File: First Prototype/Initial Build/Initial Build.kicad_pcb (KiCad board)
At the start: 2 copper layers, 33 parts, among them J2 Conn_02x04_Odd_Even, Q1 MPSA44, Q2 BC328, Q3 BC517, U1 TLC555xP, U2 TLC555xP

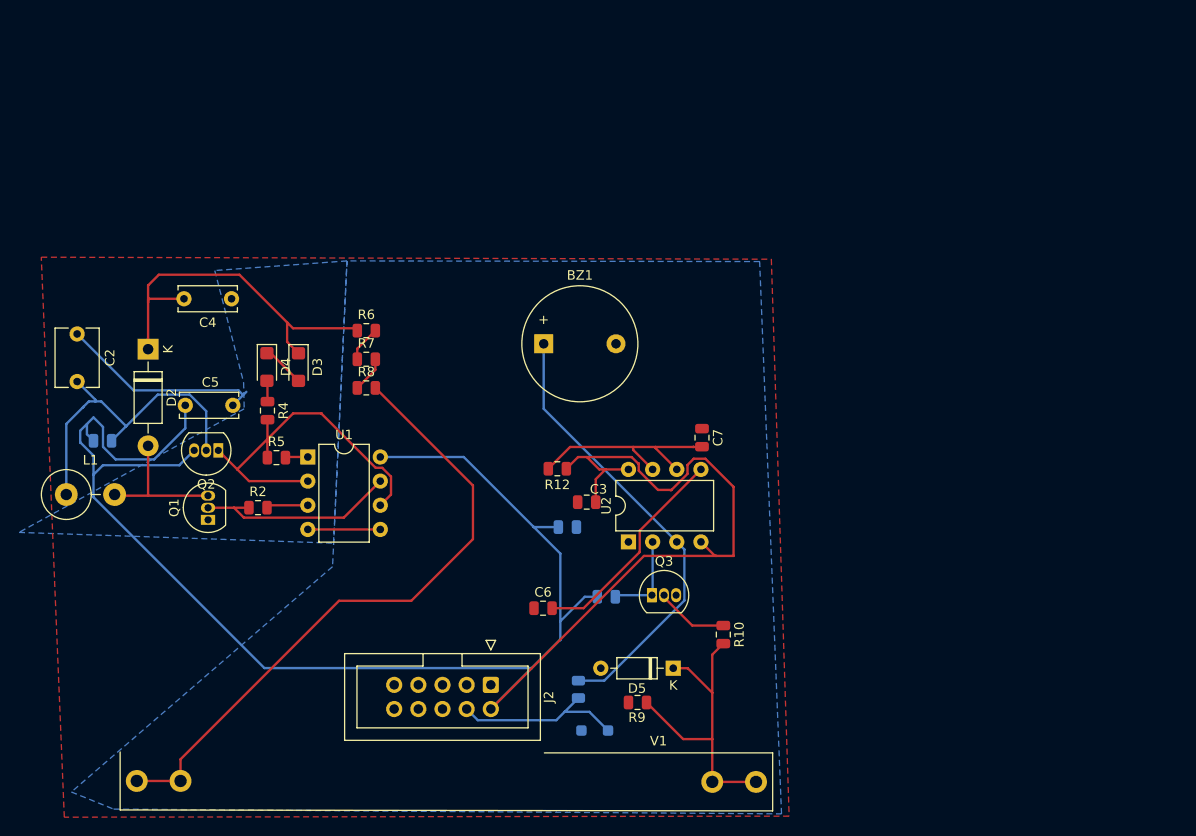
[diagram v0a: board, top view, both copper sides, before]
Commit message: updated tube fp began routing
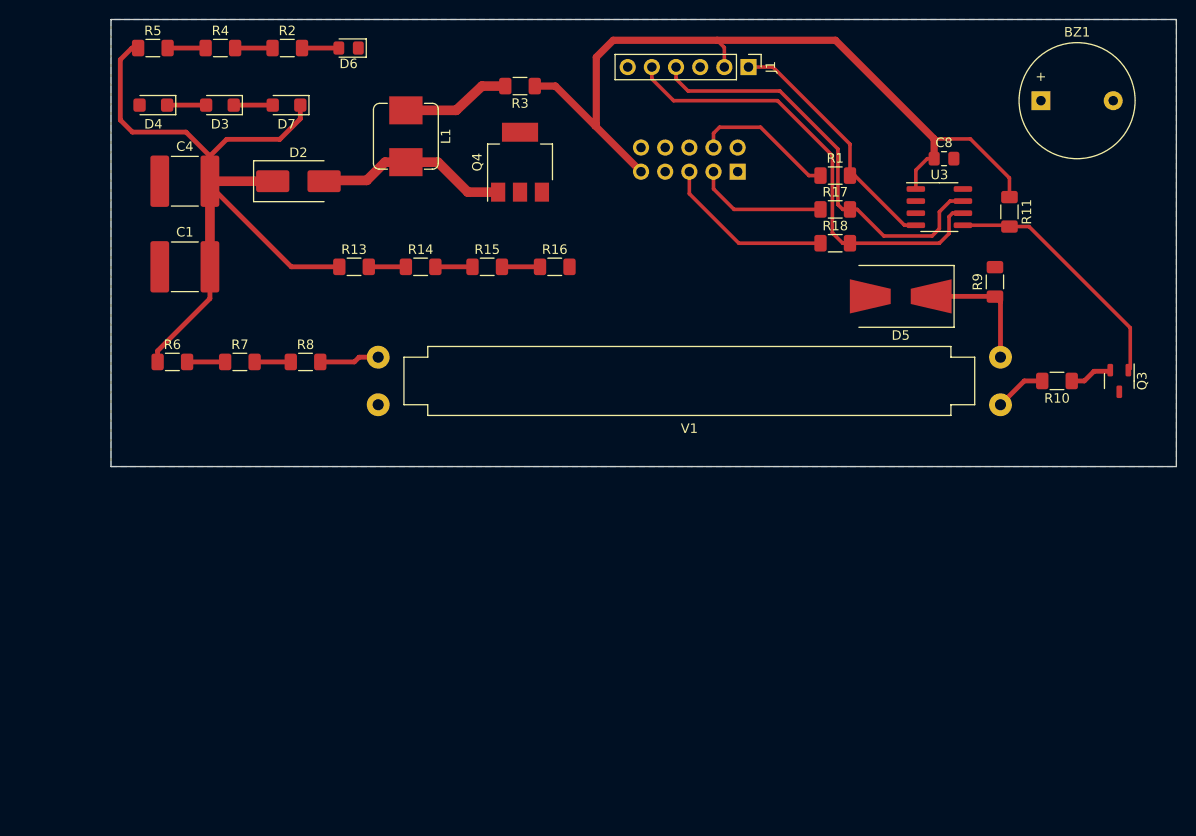
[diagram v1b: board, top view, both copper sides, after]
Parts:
- removed C2: 100n, Capacitor_THT:C_Disc_D6.0mm_W4.4mm_P5.00mm
- removed C3, C6, C7: 100n, Capacitor_SMD:C_0805_2012Metric
- removed C5: 100u, Capacitor_THT:C_Disc_D6.0mm_W2.5mm_P5.00mm
- removed D1: 3v3, Diode_SMD:D_SOD-123F
- removed Q1: MPSA44, Package_TO_SOT_THT:TO-92_Inline
- removed Q2: BC328, Package_TO_SOT_THT:TO-92_Inline
- removed R12: 3k9, Capacitor_SMD:C_0805_2012Metric
- removed U1, U2: TLC555xP, Package_DIP:DIP-8_W7.62mm
- added C8: .1u, Capacitor_SMD:C_0805_2012Metric_Pad1.18x1.45mm_HandSolder, F.Cu at (180.6, 87.6)
- added D6: APTD2012LSURCK, LED_SMD:LED_0805_2012Metric_Pad1.15x1.40mm_HandSolder, F.Cu at (118.0, 76.0)
- added D7: BZD27C150P-E3-08, Diode_SMD:D_SMF, F.Cu at (111.5, 82.0)
- added J1: Conn_01x06, Connector_PinHeader_2.54mm:PinHeader_1x06_P2.54mm_Vertical, F.Cu at (160.0, 78.0)
- added Q4: BSP135H6327XTSA1, Package_TO_SOT_SMD:SOT-223, F.Cu at (136.0, 88.0)
- added R13: 330k, Resistor_SMD:R_1206_3216Metric_Pad1.30x1.75mm_HandSolder, F.Cu at (118.5, 99.0)
- added R14: 330k, Resistor_SMD:R_1206_3216Metric_Pad1.30x1.75mm_HandSolder, F.Cu at (125.5, 99.0)
- added R15: 330k, Resistor_SMD:R_1206_3216Metric_Pad1.30x1.75mm_HandSolder, F.Cu at (132.6, 99.0)
- added R16: 3k9, Resistor_SMD:R_1206_3216Metric_Pad1.30x1.75mm_HandSolder, F.Cu at (139.7, 99.0)
- added R17: 10k, Resistor_SMD:R_1206_3216Metric_Pad1.30x1.75mm_HandSolder, F.Cu at (169.1, 93.0)
- added R18: 10k, Resistor_SMD:R_1206_3216Metric_Pad1.30x1.75mm_HandSolder, F.Cu at (169.1, 96.5)
- added U3: PIC12F1572T-I/SN, Package_SO:SOIC-8_3.9x4.9mm_P1.27mm, F.Cu at (180.1, 92.7)
- C1: value 100n -> LDEPD2100KA5N00; footprint Capacitor_SMD:C_0805_2012Metric -> Capacitor_SMD:C_2220_5650Metric_Pad1.97x5.40mm_HandSolder; moved to F.Cu
- C4: value 47n -> LDEPD2100KA5N00; footprint Capacitor_THT:C_Disc_D6.0mm_W2.5mm_P5.00mm -> Capacitor_SMD:C_2220_5650Metric_Pad1.97x5.40mm_HandSolder
- D2: value MUR160 -> MURS160-13-F; footprint Diode_THT:D_DO-41_SOD81_P10.16mm_Horizontal -> Diode_SMD:D_SMB_Handsoldering
- D3, D4: value 200v -> BZD27C150P-E3-08
- D5: footprint Diode_THT:D_DO-35_SOD27_P7.62mm_Horizontal -> Diode_SMD:D_SMB-SMC_Universal_Handsoldering
- J2: value Conn_02x04_Odd_Even -> Conn_01x10_Pin; footprint Connector_IDC:IDC-Header_2x05_P2.54mm_Vertical -> Connector_PinHeader_2.54mm:PinHeader_2x05_P2.54mm_Vertical; moved to B.Cu
- L1: value 10m -> SRR6603-103ML; footprint Inductor_THT:L_Axial_L12.0mm_D5.0mm_P5.08mm_Vertical_Fastron_MISC -> Inductor_SMD:L_Bourns_SRP7028A_7.3x6.6mm
- Q3: value BC517 -> MMBT3904-7-F; footprint Package_TO_SOT_THT:TO-92_Inline -> Package_TO_SOT_SMD:SOT-23-3
- R1: value 3k3 -> 10k; footprint Resistor_SMD:R_0805_2012Metric -> Resistor_SMD:R_1206_3216Metric_Pad1.30x1.75mm_HandSolder; moved to F.Cu
- R10, R6, R7, R8, R9: footprint Capacitor_SMD:C_0805_2012Metric -> Resistor_SMD:R_1206_3216Metric_Pad1.30x1.75mm_HandSolder
- R11, R3: footprint Capacitor_SMD:C_0805_2012Metric -> Resistor_SMD:R_1206_3216Metric_Pad1.30x1.75mm_HandSolder; moved to F.Cu
- R2: value 1k5 -> 1M8; footprint Capacitor_SMD:C_0805_2012Metric -> Resistor_SMD:R_1206_3216Metric_Pad1.30x1.75mm_HandSolder
- R4: value 10k -> 1M8; footprint Capacitor_SMD:C_0805_2012Metric -> Resistor_SMD:R_1206_3216Metric_Pad1.30x1.75mm_HandSolder
- R5: value 100k -> 1M8; footprint Capacitor_SMD:C_0805_2012Metric -> Resistor_SMD:R_1206_3216Metric_Pad1.30x1.75mm_HandSolder
- V1: value Nuclear-Radiation_Detector -> J302; footprint Geiger:Geiger Clips -> Geiger:Geiger_Clips
- moved R1 60.4 mm to (169.1, 89.4), turned to 0 degrees
- moved J2 59.9 mm to (158.9, 89.0), turned to 90 degrees
- moved R11 58.6 mm to (187.5, 93.2), turned to -90 degrees
- moved BZ1 58.2 mm to (190.8, 81.5)
- moved R9 58.0 mm to (185.9, 100.6), turned to 90 degrees
- moved R3 57.6 mm to (136.0, 80.0), turned to 180 degrees
- moved Q3 54.0 mm to (199.0, 111.0), turned to -90 degrees
- moved L1 51.9 mm to (124.0, 85.3), turned to -90 degrees
- moved C1 48.6 mm to (100.8, 99.0), turned to 0 degrees
- moved R2 48.4 mm to (111.5, 76.0)
- moved D5 45.8 mm to (176.0, 102.1)
- moved R5 45.0 mm to (97.4, 76.0)
- moved V1 44.3 mm to (153.8, 111.0)
- moved R10 44.1 mm to (192.4, 111.0), turned to 180 degrees
- moved R4 38.4 mm to (104.5, 76.0), turned to 0 degrees
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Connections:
- C1 pad 2: +3.3VA -> 400V
- D3 pad 1: 400V -> Net-(D3-K)
- D4 pad 2: Net-(D4-A) -> GND
- J2 pad 10: (no net) -> GND
- J2 pad 3: unconnected-(J2-GPIO_2-Pad3) -> USART_TX
- J2 pad 4: Net-(D1-K) -> Pulse B
- J2 pad 5: unconnected-(J2-Future-Pad5) -> USART_RX
- J2 pad 9: (no net) -> +3.3VA
- R1 pad 2: Net-(D1-K) -> Net-(J1-Pin_1)
- R2 pad 1: Net-(Q1-B) -> Net-(R2-Pad1)
- R4 pad 1: Net-(D4-A) -> Net-(R4-Pad1)
- R4 pad 2: Net-(Q2-C) -> Net-(R2-Pad1)
- R5 pad 1: Net-(Q2-C) -> 400V
- R5 pad 2: GND -> Net-(R4-Pad1)
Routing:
- net +3.3VA: track 217.2 -> 84.0 mm
- net Net-(R8-Pad2): track 67.4 -> 6.30 mm
- net Net-(J1-Pin_5): track 0.00 -> 48.2 mm
- net Net-(J1-Pin_4): track 0.00 -> 44.2 mm
- net 400V: track 39.4 -> 80.4 mm
- net Net-(Q2-C): track 39.9 -> 0.00 mm
- net Pulse B: track 47.7 -> 15.1 mm
- net Net-(J1-Pin_1): track 0.00 -> 26.4 mm
- net GND: track 24.5 -> 0.00 mm
- net Net-(L1-Pad1): track 35.7 -> 11.5 mm
- net Net-(U2-DIS): track 23.7 -> 0.00 mm
- net Net-(U2-CV): track 23.0 -> 0.00 mm
- net Net-(Q1-B): track 21.7 -> 0.00 mm
- net Net-(D1-K): track 18.6 -> 0.00 mm
- net USART_RX: track 0.00 -> 18.3 mm
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- removed copper zone on F.Cu, net GND
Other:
- board outline added: 112 x 47 mm

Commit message: finished routing
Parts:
- moved D5 18.2 mm to (194.2, 101.1), turned to 0 degrees
- moved D4 16.1 mm to (113.5, 81.0), turned to 0 degrees
- moved D7 12.6 mm to (98.9, 81.0), turned to 0 degrees
- moved R9 8.97 mm to (192.5, 106.7), turned to 0 degrees
- moved R6 7.23 mm to (106.4, 111.0)
- moved R7 4.25 mm to (110.3, 106.9)
- moved R8 2.08 mm to (114.0, 111.0)
- moved D3 1.98 mm to (106.2, 81.0), turned to 0 degrees
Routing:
- net PWM: track 0.00 -> 53.4 mm, vias 0 -> 2
- net Net-(U3-RA4): track 4.00 -> 54.3 mm, vias 0 -> 2
- net Pulse B: track 15.1 -> 41.2 mm, vias 0 -> 2
- net GND: track 0.00 -> 20.1 mm, vias 0 -> 11
- net 400V: track 80.4 -> 64.3 mm
- net +3.3VA: track 84.0 -> 91.9 mm
- net Pulse A: track 26.6 -> 31.2 mm
- net Net-(D5-K): track 18.8 -> 15.7 mm
- net Net-(J1-Pin_1): track 26.4 -> 27.7 mm
- net Net-(R7-Pad2): track 3.80 -> 4.38 mm
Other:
- board text added: "400VDC"
- board text added: "CHARGED"
